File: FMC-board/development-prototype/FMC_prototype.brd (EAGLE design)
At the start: 103.8 x 69.8 mm, 69 parts, among them J1 DC_POWER_JACK-PJ-102AH, J2 DC_POWER_JACK-PJ-102AH

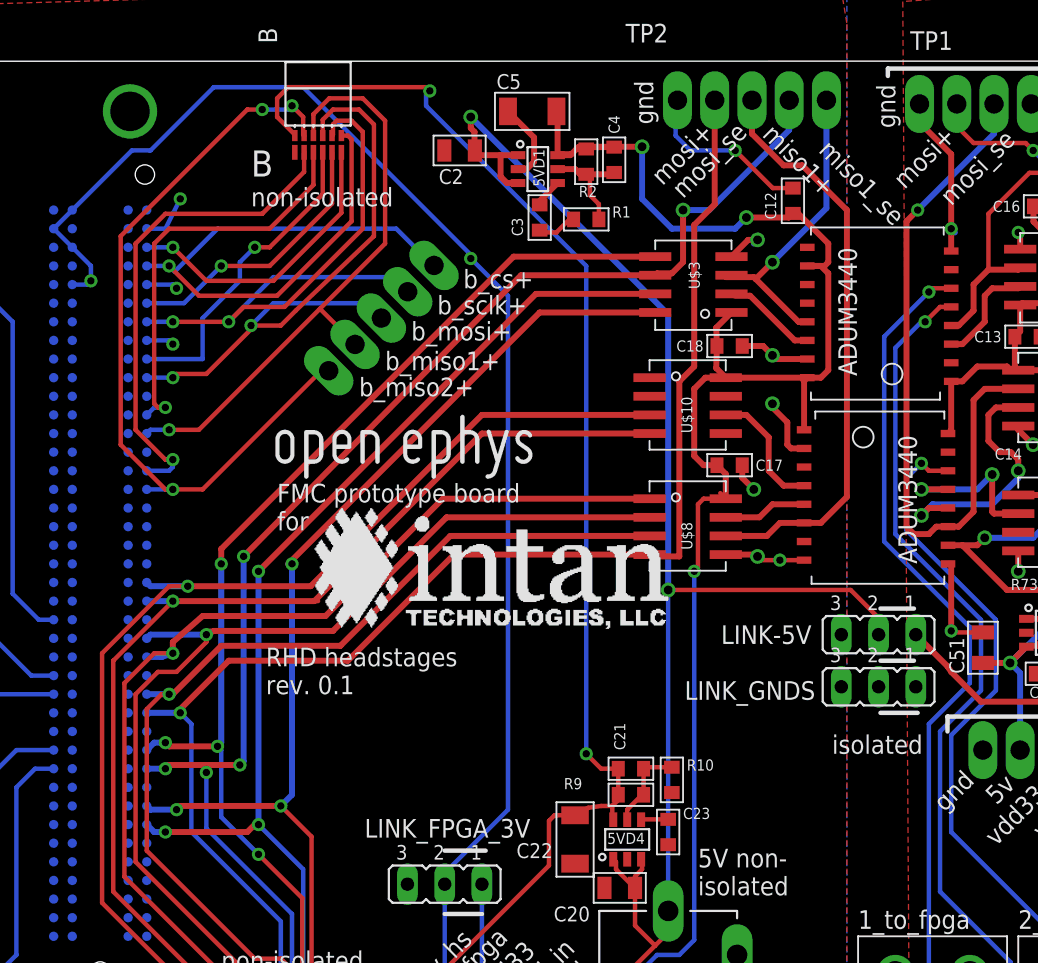
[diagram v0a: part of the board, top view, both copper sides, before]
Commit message: routed isolated testpoints
likely still errors in there
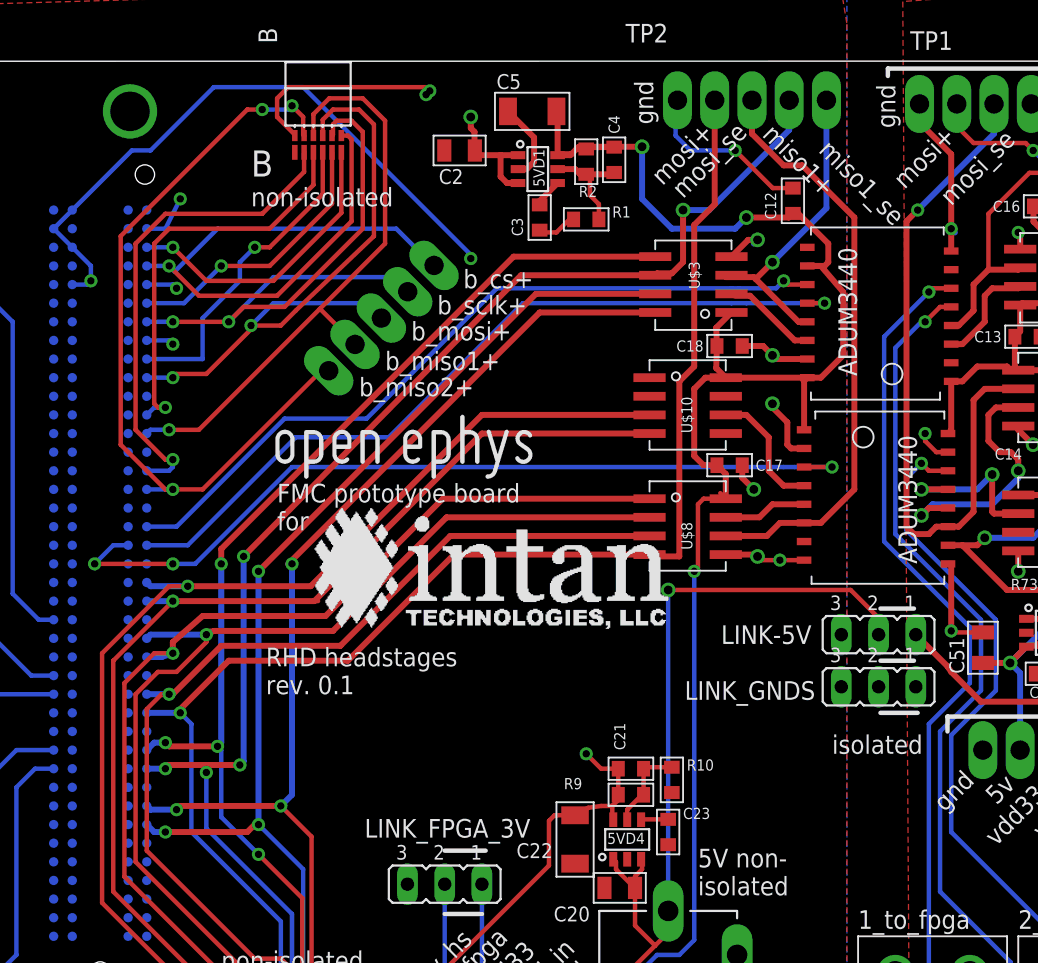
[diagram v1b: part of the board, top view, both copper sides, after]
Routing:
- net TP3_FROM_FPGA: track 0.00 -> 57.7 mm, vias 0 -> 3
- net TP1_TO_FPGA: track 0.00 -> 54.2 mm, vias 0 -> 1
- net TP2_TO_FPGA: track 0.00 -> 52.1 mm, vias 0 -> 1
- net GND_ISOLATED: track 44.7 -> 48.2 mm, vias 11 -> 12
- net VDD33: track 134.1 -> 134.8 mm
- net VDD_IN: track 109.3 -> 109.8 mm
- net VDD36: vias 2 -> 3
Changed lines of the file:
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@@
 <grid distance="0.01" unitdist="inch" unit="inch" style="lines" multiple="1" display="yes" altdistance="0.0125" altunitdist="inch" altunit="inch"/>
 <layers>
-<layer number="1" name="Top" color="4" fill="1" visible="yes" active="yes"/>
+<layer number="1" name="Top" color="12" fill="1" visible="yes" active="yes"/>
 <layer number="2" name="$GND" color="2" fill="1" visible="no" active="yes"/>
 <layer number="15" name="$VCC" color="3" fill="1" visible="no" active="yes"/>
@@
 <wire x1="23.368" y1="50.546" x2="23.622" y2="50.546" width="0.3048" layer="2"/>
 <wire x1="23.622" y1="50.546" x2="23.876" y2="50.8" width="0.3048" layer="2"/>
+<wire x1="21.59" y1="27.94" x2="21.59" y2="31.75" width="0" layer="19" extent="16-16"/>
 <wire x1="21.59" y1="24.13" x2="21.59" y2="27.94" width="0" layer="19" extent="16-16"/>
-<wire x1="21.59" y1="31.75" x2="21.59" y2="27.94" width="0" layer="19" extent="16-16"/>
+<wire x1="21.59" y1="39.37" x2="21.59" y2="35.56" width="0" layer="19" extent="16-16"/>
 </signal>
 <signal name="MISO2+">
@@
 <wire x1="62.865" y1="64.897" x2="65.024" y2="62.738" width="0.4064" layer="1"/>
 <wire x1="65.024" y1="62.738" x2="66.294" y2="62.738" width="0.4064" layer="1"/>
-<wire x1="66.294" y1="62.738" x2="69.342" y2="59.69" width="0.4064" layer="1"/>
-<wire x1="69.342" y1="59.69" x2="69.342" y2="40.132" width="0.4064" layer="1"/>
-<wire x1="69.342" y1="40.132" x2="67.564" y2="38.354" width="0.4064" layer="1"/>
+<wire x1="66.294" y1="62.738" x2="69.85" y2="59.182" width="0.4064" layer="1"/>
+<wire x1="69.85" y1="59.182" x2="69.85" y2="40.64" width="0.4064" layer="1"/>
+<wire x1="69.85" y1="40.64" x2="67.564" y2="38.354" width="0.4064" layer="1"/>
 <wire x1="67.564" y1="38.354" x2="66.421" y2="38.354" width="0.4064" layer="1"/>
 </signal>
@@
 <contactref element="U$19" pad="GND$3"/>
 <contactref element="U$19" pad="GND$4"/>
-<wire x1="81.026" y1="44.704" x2="76.235" y2="43.18" width="0" layer="19" extent="1-1"/>
+<wire x1="76.235" y1="43.18" x2="75.438" y2="43.18" width="0.3048" layer="1"/>
+<wire x1="75.438" y1="43.18" x2="74.676" y2="43.942" width="0.3048" layer="1"/>
+<wire x1="74.676" y1="43.942" x2="74.676" y2="44.45" width="0.3048" layer="1"/>
+<via x="74.676" y="44.45" extent="1-16" drill="0.5"/>
+<wire x1="74.676" y1="44.45" x2="74.93" y2="44.704" width="0.3048" layer="2"/>
+<wire x1="74.93" y1="44.704" x2="74.93" y2="45.466" width="0.3048" layer="2"/>
 </signal>
 <signal name="VDD_ISOLATED">
@@
 <wire x1="67.818" y1="55.88" x2="66.64" y2="55.88" width="0.4064" layer="1"/>
 <wire x1="66.64" y1="55.88" x2="67.564" y2="55.88" width="0.4064" layer="1"/>
-<wire x1="67.564" y1="55.88" x2="68.072" y2="55.372" width="0.4064" layer="1"/>
-<wire x1="68.072" y1="55.372" x2="68.072" y2="48.768" width="0.4064" layer="1"/>
-<wire x1="68.072" y1="48.768" x2="67.564" y2="48.26" width="0.4064" layer="1"/>
+<wire x1="67.564" y1="55.88" x2="69.088" y2="54.102" width="0.4064" layer="1"/>
+<wire x1="69.088" y1="54.102" x2="69.088" y2="49.784" width="0.4064" layer="1"/>
+<wire x1="69.088" y1="49.784" x2="67.564" y2="48.26" width="0.4064" layer="1"/>
 <wire x1="67.564" y1="48.26" x2="66.64" y2="48.26" width="0.4064" layer="1"/>
 <wire x1="66.421" y1="44.704" x2="66.421" y2="48.041" width="0.4064" layer="1"/>
@@
 <wire x1="43.942" y1="63.7794" x2="43.9674" y2="63.754" width="0.4064" layer="1"/>
 <via x="57.15" y="33.782" extent="1-16" drill="0.6"/>
-<wire x1="57.15" y1="33.782" x2="57.15" y2="52.578" width="0.4064" layer="16"/>
-<wire x1="57.15" y1="52.578" x2="43.688" y2="66.04" width="0.4064" layer="16"/>
 <via x="43.688" y="66.04" extent="1-16" drill="0.6"/>
 <wire x1="43.688" y1="66.04" x2="43.688" y2="65.278" width="0.4064" layer="1"/>
@@
 <wire x1="54.8894" y1="13.462" x2="54.8894" y2="10.8966" width="0.3048" layer="1"/>
 <wire x1="54.8894" y1="10.8966" x2="56.261" y2="9.525" width="0.3048" layer="1"/>
+<wire x1="43.688" y1="66.04" x2="57.15" y2="52.578" width="0.6096" layer="15"/>
+<wire x1="57.15" y1="52.578" x2="57.15" y2="33.782" width="0.6096" layer="15"/>
+<wire x1="57.15" y1="33.274" x2="57.15" y2="33.782" width="0.6096" layer="15"/>
 </signal>
 <signal name="5V_ISOLATED">
@@
 <wire x1="21.844" y1="63.754" x2="20.574" y2="63.754" width="0.3048" layer="16"/>
 <wire x1="20.574" y1="63.754" x2="16.51" y2="59.69" width="0.3048" layer="16"/>
-<wire x1="43.688" y1="56.388" x2="46.228" y2="53.848" width="0.3048" layer="16"/>
-<wire x1="46.228" y1="53.848" x2="46.228" y2="18.796" width="0.3048" layer="16"/>
-<wire x1="46.228" y1="18.796" x2="41.91" y2="14.478" width="0.3048" layer="16"/>
 <wire x1="41.656" y1="14.478" x2="41.91" y2="14.478" width="0.3048" layer="16"/>
+<wire x1="43.688" y1="56.388" x2="45.466" y2="54.61" width="0.6096" layer="15"/>
+<wire x1="45.466" y1="54.61" x2="45.466" y2="19.05" width="0.6096" layer="15"/>
+<wire x1="45.466" y1="19.05" x2="41.91" y2="15.494" width="0.6096" layer="15"/>
+<wire x1="41.91" y1="15.494" x2="41.91" y2="13.716" width="0.6096" layer="15"/>
 </signal>
 <signal name="N$3">
@@
 <wire x1="52.578" y1="21.59" x2="51.562" y2="22.606" width="0.3048" layer="1"/>
 <via x="51.562" y="22.606" extent="1-16" drill="0.5"/>
-<wire x1="51.562" y1="22.606" x2="51.562" y2="55.88" width="0.3048" layer="16"/>
-<wire x1="51.562" y1="55.88" x2="40.64" y2="66.802" width="0.3048" layer="16"/>
-<wire x1="40.64" y1="66.802" x2="40.64" y2="67.564" width="0.3048" layer="16"/>
 <wire x1="40.64" y1="67.564" x2="40.894" y2="67.818" width="0.3048" layer="16"/>
 <via x="40.894" y="67.818" extent="1-16" drill="0.5"/>
@@
 <wire x1="31.242" y1="68.072" x2="40.64" y2="68.072" width="0.3048" layer="1"/>
 <wire x1="40.64" y1="68.072" x2="40.894" y2="67.818" width="0.3048" layer="1"/>
+<via x="40.64" y="67.564" extent="1-16" drill="0.5"/>
+<wire x1="40.64" y1="67.564" x2="40.894" y2="67.31" width="0.6096" layer="15"/>
+<wire x1="40.894" y1="67.31" x2="40.894" y2="64.516" width="0.6096" layer="15"/>
+<wire x1="40.894" y1="64.516" x2="51.562" y2="53.848" width="0.6096" layer="15"/>
+<wire x1="51.562" y1="53.848" x2="51.562" y2="22.606" width="0.6096" layer="15"/>
 </signal>
 <signal name="N$14">
@@
 <contactref element="U$11" pad="P12"/>
 <contactref element="U$4" pad="P$22"/>
-<wire x1="21.59" y1="36.83" x2="66.64" y2="53.34" width="0" layer="19" extent="1-16"/>
+<wire x1="66.64" y1="53.34" x2="67.818" y2="53.34" width="0.3048" layer="1"/>
+<via x="67.818" y="53.34" extent="1-16" drill="0.5"/>
+<wire x1="67.818" y1="53.34" x2="62.484" y2="53.34" width="0.3048" layer="16"/>
+<wire x1="62.484" y1="53.34" x2="61.468" y2="53.34" width="0.3048" layer="16"/>
+<wire x1="21.59" y1="36.83" x2="24.384" y2="36.83" width="0.3048" layer="16"/>
+<wire x1="24.384" y1="36.83" x2="31.75" y2="44.196" width="0.3048" layer="16"/>
+<wire x1="31.75" y1="44.196" x2="38.1" y2="44.196" width="0.3048" layer="16"/>
+<wire x1="38.1" y1="44.196" x2="47.244" y2="53.34" width="0.3048" layer="16"/>
+<wire x1="47.244" y1="53.34" x2="61.468" y2="53.34" width="0.3048" layer="16"/>
 </signal>
 <signal name="TP2_TO_FPGA">
 <contactref element="U$11" pad="P11"/>
 <contactref element="U$4" pad="P$23"/>
-<wire x1="21.59" y1="38.1" x2="66.64" y2="54.61" width="0" layer="19" extent="1-16"/>
+<wire x1="66.64" y1="54.61" x2="65.278" y2="54.61" width="0.3048" layer="1"/>
+<wire x1="65.278" y1="54.61" x2="65.024" y2="54.864" width="0.3048" layer="1"/>
+<via x="65.024" y="54.864" extent="1-16" drill="0.5"/>
+<wire x1="65.024" y1="54.864" x2="64.516" y2="54.356" width="0.3048" layer="16"/>
+<wire x1="64.516" y1="54.356" x2="61.976" y2="54.356" width="0.3048" layer="16"/>
+<wire x1="61.976" y1="54.356" x2="61.468" y2="54.356" width="0.3048" layer="16"/>
+<wire x1="21.59" y1="38.1" x2="23.622" y2="38.1" width="0.3048" layer="16"/>
+<wire x1="23.622" y1="38.1" x2="30.988" y2="45.466" width="0.3048" layer="16"/>
+<wire x1="30.988" y1="45.466" x2="36.576" y2="45.466" width="0.3048" layer="16"/>
+<wire x1="36.576" y1="45.466" x2="45.466" y2="54.356" width="0.3048" layer="16"/>
+<wire x1="45.466" y1="54.356" x2="61.468" y2="54.356" width="0.3048" layer="16"/>
 </signal>
 <signal name="TP3_TO_SMA">
@@
 <contactref element="U$12" pad="P3"/>
 <contactref element="U$4" pad="P$62"/>
-<wire x1="20.32" y1="36.83" x2="66.421" y2="42.164" width="0" layer="19" extent="1-16"/>
+<wire x1="66.421" y1="42.164" x2="68.326" y2="42.164" width="0.3048" layer="1"/>
+<via x="68.326" y="42.164" extent="1-16" drill="0.5"/>
+<wire x1="68.326" y1="42.164" x2="65.786" y2="42.164" width="0.3048" layer="16"/>
+<wire x1="65.786" y1="42.164" x2="65.024" y2="42.164" width="0.3048" layer="16"/>
+<wire x1="20.32" y1="36.83" x2="19.304" y2="36.83" width="0.3048" layer="16"/>
+<wire x1="19.304" y1="36.83" x2="18.034" y2="35.56" width="0.3048" layer="16"/>
+<via x="18.034" y="35.56" extent="1-16" drill="0.5"/>
+<wire x1="18.034" y1="35.56" x2="23.368" y2="35.56" width="0.3048" layer="1"/>
+<via x="23.368" y="35.56" extent="1-16" drill="0.5"/>
+<wire x1="23.368" y1="35.56" x2="24.892" y2="35.56" width="0.3048" layer="16"/>
+<wire x1="24.892" y1="35.56" x2="31.496" y2="42.164" width="0.3048" layer="16"/>
+<wire x1="31.496" y1="42.164" x2="65.024" y2="42.164" width="0.3048" layer="16"/>
 </signal>
 <signal name="TP4">

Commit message: more cleanup
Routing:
- net VDD36: track 99.5 -> 95.8 mm, vias 3 -> 2
- net 3V_FPGA: track 99.7 -> 96.1 mm
- net TP3_FROM_FPGA: track 57.7 -> 56.7 mm
- net B_MISO2+: track 53.1 -> 52.3 mm, vias 3 -> 1
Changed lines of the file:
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@@
 <layer number="1" name="Top" color="12" fill="1" visible="yes" active="yes"/>
 <layer number="2" name="$GND" color="2" fill="1" visible="no" active="yes"/>
-<layer number="15" name="$VCC" color="3" fill="1" visible="no" active="yes"/>
+<layer number="15" name="$VCC" color="3" fill="1" visible="yes" active="yes"/>
 <layer number="16" name="Bottom" color="1" fill="1" visible="yes" active="yes"/>
 <layer number="17" name="Pads" color="2" fill="1" visible="yes" active="yes"/>
@@
 <text x="70.104" y="10.668" size="1.27" layer="25" font="vector" ratio="15">1_to_fpga</text>
 <text x="81.026" y="10.668" size="1.27" layer="25" font="vector" ratio="15">2_to_fpga</text>
-<text x="92.202" y="10.414" size="1.27" layer="25" font="vector" ratio="15">3_from_fpga</text>
+<text x="91.694" y="10.414" size="1.27" layer="25" font="vector" ratio="15">3_from_fpga</text>
 </plain>
 <attributes>
@@
 <wire x1="23.368" y1="50.546" x2="23.622" y2="50.546" width="0.3048" layer="2"/>
 <wire x1="23.622" y1="50.546" x2="23.876" y2="50.8" width="0.3048" layer="2"/>
-<wire x1="21.59" y1="27.94" x2="21.59" y2="31.75" width="0" layer="19" extent="16-16"/>
 <wire x1="21.59" y1="24.13" x2="21.59" y2="27.94" width="0" layer="19" extent="16-16"/>
+<wire x1="21.59" y1="31.75" x2="21.59" y2="27.94" width="0" layer="19" extent="16-16"/>
 <wire x1="21.59" y1="39.37" x2="21.59" y2="35.56" width="0" layer="19" extent="16-16"/>
 </signal>
@@
 <wire x1="41.656" y1="14.478" x2="41.91" y2="13.716" width="0.3048" layer="16"/>
 <wire x1="43.688" y1="56.388" x2="43.688" y2="56.642" width="0.3048" layer="16"/>
-<wire x1="43.688" y1="56.642" x2="32.258" y2="68.072" width="0.3048" layer="16"/>
-<wire x1="32.258" y1="68.072" x2="26.162" y2="68.072" width="0.3048" layer="16"/>
-<wire x1="26.162" y1="68.072" x2="21.844" y2="63.754" width="0.3048" layer="16"/>
-<wire x1="21.844" y1="63.754" x2="20.574" y2="63.754" width="0.3048" layer="16"/>
+<wire x1="43.688" y1="56.642" x2="36.576" y2="63.754" width="0.3048" layer="16"/>
+<wire x1="36.576" y1="63.754" x2="20.574" y2="63.754" width="0.3048" layer="16"/>
 <wire x1="20.574" y1="63.754" x2="16.51" y2="59.69" width="0.3048" layer="16"/>
 <wire x1="41.656" y1="14.478" x2="41.91" y2="14.478" width="0.3048" layer="16"/>
@@
 <wire x1="52.578" y1="21.59" x2="51.562" y2="22.606" width="0.3048" layer="1"/>
 <via x="51.562" y="22.606" extent="1-16" drill="0.5"/>
-<wire x1="40.64" y1="67.564" x2="40.894" y2="67.818" width="0.3048" layer="16"/>
-<via x="40.894" y="67.818" extent="1-16" drill="0.5"/>
 <wire x1="33.4645" y1="5.08" x2="39.116" y2="5.08" width="0.3048" layer="1"/>
 <wire x1="39.116" y1="5.08" x2="39.624" y2="4.572" width="0.3048" layer="1"/>
-<wire x1="31.6865" y1="64.77" x2="31.6865" y2="64.8335" width="0.3048" layer="1"/>
-<wire x1="31.6865" y1="64.8335" x2="30.48" y2="66.04" width="0.3048" layer="1"/>
-<wire x1="30.48" y1="66.04" x2="30.48" y2="67.31" width="0.3048" layer="1"/>
-<wire x1="30.48" y1="67.31" x2="31.242" y2="68.072" width="0.3048" layer="1"/>
-<wire x1="31.242" y1="68.072" x2="40.64" y2="68.072" width="0.3048" layer="1"/>
-<wire x1="40.64" y1="68.072" x2="40.894" y2="67.818" width="0.3048" layer="1"/>
-<via x="40.64" y="67.564" extent="1-16" drill="0.5"/>
-<wire x1="40.64" y1="67.564" x2="40.894" y2="67.31" width="0.6096" layer="15"/>
-<wire x1="40.894" y1="67.31" x2="40.894" y2="64.516" width="0.6096" layer="15"/>
-<wire x1="40.894" y1="64.516" x2="51.562" y2="53.848" width="0.6096" layer="15"/>
+<wire x1="40.64" y1="64.77" x2="51.562" y2="53.848" width="0.6096" layer="15"/>
 <wire x1="51.562" y1="53.848" x2="51.562" y2="22.606" width="0.6096" layer="15"/>
+<wire x1="31.6865" y1="64.77" x2="29.718" y2="64.77" width="0.3048" layer="1"/>
+<via x="29.718" y="64.77" extent="1-16" drill="0.5"/>
+<wire x1="29.718" y1="64.77" x2="30.099" y2="64.897" width="0.3048" layer="15"/>
+<wire x1="40.64" y1="64.77" x2="29.718" y2="64.77" width="0.6096" layer="15"/>
 </signal>
 <signal name="N$14">
@@
 <contactref element="U$4" pad="P$25"/>
 <contactref element="B" pad="B5"/>
-<wire x1="31.75" y1="66.548" x2="31.496" y2="66.802" width="0.3048" layer="16"/>
-<via x="31.496" y="66.802" extent="1-16" drill="0.5"/>
-<wire x1="31.496" y1="66.802" x2="32.258" y2="66.04" width="0.3048" layer="1"/>
 <wire x1="32.258" y1="66.04" x2="32.258" y2="64.8335" width="0.3048" layer="1"/>
 <wire x1="32.258" y1="64.8335" x2="32.3215" y2="64.77" width="0.3048" layer="1"/>
-<wire x1="31.75" y1="66.548" x2="29.464" y2="66.548" width="0.3048" layer="16"/>
-<via x="29.464" y="66.548" extent="1-16" drill="0.5"/>
-<wire x1="29.464" y1="66.548" x2="28.448" y2="66.548" width="0.3048" layer="1"/>
 <wire x1="28.448" y1="66.548" x2="19.812" y2="57.912" width="0.3048" layer="1"/>
 <wire x1="19.812" y1="57.912" x2="19.812" y2="43.688" width="0.3048" layer="1"/>
@@
 <wire x1="33.491896875" y1="48.731896875" x2="25.4" y2="40.64" width="0.3048" layer="1"/>
 <wire x1="25.4" y1="40.64" x2="23.368" y2="40.64" width="0.3048" layer="1"/>
+<wire x1="32.258" y1="66.04" x2="31.75" y2="66.548" width="0.3048" layer="1"/>
+<wire x1="31.75" y1="66.548" x2="28.448" y2="66.548" width="0.3048" layer="1"/>
 </signal>
 <signal name="B_MISO2-">
@@
 <wire x1="66.64" y1="53.34" x2="67.818" y2="53.34" width="0.3048" layer="1"/>
 <via x="67.818" y="53.34" extent="1-16" drill="0.5"/>
-<wire x1="67.818" y1="53.34" x2="62.484" y2="53.34" width="0.3048" layer="16"/>
-<wire x1="62.484" y1="53.34" x2="61.468" y2="53.34" width="0.3048" layer="16"/>
-<wire x1="21.59" y1="36.83" x2="24.384" y2="36.83" width="0.3048" layer="16"/>
-<wire x1="24.384" y1="36.83" x2="31.75" y2="44.196" width="0.3048" layer="16"/>
-<wire x1="31.75" y1="44.196" x2="38.1" y2="44.196" width="0.3048" layer="16"/>
-<wire x1="38.1" y1="44.196" x2="47.244" y2="53.34" width="0.3048" layer="16"/>
-<wire x1="47.244" y1="53.34" x2="61.468" y2="53.34" width="0.3048" layer="16"/>
+<wire x1="21.59" y1="36.83" x2="23.368" y2="36.83" width="0.3048" layer="16"/>
+<wire x1="23.368" y1="36.83" x2="30.734" y2="44.196" width="0.3048" layer="16"/>
+<wire x1="30.734" y1="44.196" x2="36.576" y2="44.196" width="0.3048" layer="16"/>
+<wire x1="36.576" y1="44.196" x2="45.72" y2="53.34" width="0.3048" layer="16"/>
+<wire x1="45.72" y1="53.34" x2="67.818" y2="53.34" width="0.3048" layer="16"/>
 </signal>
 <signal name="TP2_TO_FPGA">
@@
 <wire x1="65.278" y1="54.61" x2="65.024" y2="54.864" width="0.3048" layer="1"/>
 <via x="65.024" y="54.864" extent="1-16" drill="0.5"/>
-<wire x1="65.024" y1="54.864" x2="64.516" y2="54.356" width="0.3048" layer="16"/>
-<wire x1="64.516" y1="54.356" x2="61.976" y2="54.356" width="0.3048" layer="16"/>
-<wire x1="61.976" y1="54.356" x2="61.468" y2="54.356" width="0.3048" layer="16"/>
 <wire x1="21.59" y1="38.1" x2="23.622" y2="38.1" width="0.3048" layer="16"/>
-<wire x1="23.622" y1="38.1" x2="30.988" y2="45.466" width="0.3048" layer="16"/>
-<wire x1="30.988" y1="45.466" x2="36.576" y2="45.466" width="0.3048" layer="16"/>
-<wire x1="36.576" y1="45.466" x2="45.466" y2="54.356" width="0.3048" layer="16"/>
-<wire x1="45.466" y1="54.356" x2="61.468" y2="54.356" width="0.3048" layer="16"/>
+<wire x1="23.622" y1="38.1" x2="30.48" y2="44.958" width="0.3048" layer="16"/>
+<wire x1="30.48" y1="44.958" x2="36.068" y2="44.958" width="0.3048" layer="16"/>
+<wire x1="36.068" y1="44.958" x2="45.974" y2="54.864" width="0.3048" layer="16"/>
+<wire x1="45.974" y1="54.864" x2="65.024" y2="54.864" width="0.3048" layer="16"/>
 </signal>
 <signal name="TP3_TO_SMA">
@@
 <wire x1="66.421" y1="42.164" x2="68.326" y2="42.164" width="0.3048" layer="1"/>
 <via x="68.326" y="42.164" extent="1-16" drill="0.5"/>
-<wire x1="68.326" y1="42.164" x2="65.786" y2="42.164" width="0.3048" layer="16"/>
-<wire x1="65.786" y1="42.164" x2="65.024" y2="42.164" width="0.3048" layer="16"/>
 <wire x1="20.32" y1="36.83" x2="19.304" y2="36.83" width="0.3048" layer="16"/>
-<wire x1="19.304" y1="36.83" x2="18.034" y2="35.56" width="0.3048" layer="16"/>
-<via x="18.034" y="35.56" extent="1-16" drill="0.5"/>
-<wire x1="18.034" y1="35.56" x2="23.368" y2="35.56" width="0.3048" layer="1"/>
+<wire x1="19.304" y1="36.83" x2="18.542" y2="36.068" width="0.3048" layer="16"/>
+<via x="18.542" y="36.068" extent="1-16" drill="0.5"/>
+<wire x1="18.542" y1="36.068" x2="19.304" y2="35.56" width="0.3048" layer="1"/>
+<wire x1="19.304" y1="35.56" x2="23.368" y2="35.56" width="0.3048" layer="1"/>
 <via x="23.368" y="35.56" extent="1-16" drill="0.5"/>
 <wire x1="23.368" y1="35.56" x2="24.892" y2="35.56" width="0.3048" layer="16"/>
 <wire x1="24.892" y1="35.56" x2="31.496" y2="42.164" width="0.3048" layer="16"/>
-<wire x1="31.496" y1="42.164" x2="65.024" y2="42.164" width="0.3048" layer="16"/>
+<wire x1="31.496" y1="42.164" x2="68.326" y2="42.164" width="0.3048" layer="16"/>
 </signal>
 <signal name="TP4">

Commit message: cleanup, starting DRC
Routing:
- net B_MISO2+: track 52.3 -> 51.3 mm
- net TP6: track 16.2 -> 15.5 mm
- net MOSI-_ISOLATED: track 16.4 -> 15.9 mm
